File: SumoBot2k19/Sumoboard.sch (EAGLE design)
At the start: 37 parts

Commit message: began routing on PCB, moved components around for extra clarity, learned how to align things
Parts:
- added SWITCH: (no value), SparkFun-Connectors:CONN_03
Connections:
- removed net VIN1: C10.1
- removed net VIN2: C11.1
- removed net VIN3: C12.1
- new net VBAT: BATTERY-1.S, SWITCH.1
- net LEFT_DIR: now also B1.9*/RX2; no longer B1.2
- net LEFT_PWM: now also B1.8/TX3; no longer B1.3*
- net RIGHT_DIR: now also B1.3*; no longer B1.8/TX3
- net RIGHT_PWM: now also B1.2; no longer B1.9*/RX2
- net VIN: now also C10.1, C11.1, C12.1, SWITCH.2; no longer BATTERY-1.S
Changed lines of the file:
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@@
 <part name="BATTERY" library="Rembrandt Electronics - JST XH Connectors v1-0" deviceset="JST-XH-02-PIN" device="-LONG-PAD"/>
 <part name="GND1" library="audio amplifier example" library_urn="urn:adsk.eagle:library:970892" deviceset="GND" device="" value="SUP"/>
+<part name="SWITCH" library="SparkFun-Connectors" library_urn="urn:adsk.eagle:library:513" deviceset="CONN_03" device="" package3d_urn="urn:adsk.eagle:package:38063/1"/>
 </parts>
 <sheets>
@@
 </instance>
 <instance part="GND1" gate="G$1" x="147.32" y="20.32" smashed="yes"/>
+<instance part="SWITCH" gate="J$1" x="132.08" y="40.64" smashed="yes">
+<attribute name="VALUE" x="129.54" y="33.274" size="1.778" layer="96" font="vector"/>
+<attribute name="NAME" x="129.54" y="46.228" size="1.778" layer="95" font="vector"/>
+</instance>
 </instances>
 <busses>
@@
 <junction x="78.74" y="96.52"/>
 <label x="78.74" y="96.52" size="1.778" layer="95"/>
+<pinref part="C12" gate="G$1" pin="1"/>
+<wire x1="81.28" y1="96.52" x2="78.74" y2="96.52" width="0.1524" layer="91"/>
 </segment>
 <segment>
@@
 <junction x="78.74" y="76.2"/>
 <label x="78.74" y="76.2" size="1.778" layer="95"/>
+<pinref part="C11" gate="G$1" pin="1"/>
+<wire x1="81.28" y1="76.2" x2="78.74" y2="76.2" width="0.1524" layer="91"/>
 </segment>
 <segment>
@@
 <junction x="78.74" y="55.88"/>
 <label x="78.74" y="55.88" size="1.778" layer="95"/>
+<pinref part="C10" gate="G$1" pin="1"/>
+<wire x1="81.28" y1="55.88" x2="78.74" y2="55.88" width="0.1524" layer="91"/>
 </segment>
 <segment>
@@
 </segment>
 <segment>
-<pinref part="BATTERY" gate="-1" pin="S"/>
-<junction x="147.32" y="22.86"/>
-<label x="142.24" y="22.86" size="1.778" layer="95"/>
+<pinref part="SWITCH" gate="J$1" pin="2"/>
+<junction x="139.7" y="40.64"/>
+<label x="139.7" y="40.64" size="1.778" layer="95"/>
 </segment>
 </net>
@@
 <net name="RIGHT_DIR" class="0">
 <segment>
-<pinref part="B1" gate="G$1" pin="8/TX3"/>
-<junction x="30.48" y="66.04"/>
-<label x="30.48" y="66.04" size="1.778" layer="95"/>
-<wire x1="43.18" y1="66.04" x2="30.48" y2="66.04" width="0.1524" layer="91"/>
-</segment>
-<segment>
 <pinref part="SV5" gate="G$1" pin="2"/>
 <junction x="60.96" y="60.96"/>
@@
 <label x="48.26" y="40.64" size="1.778" layer="95"/>
 <wire x1="48.26" y1="40.64" x2="60.96" y2="40.64" width="0.1524" layer="91"/>
-</segment>
-</net>
-<net name="LEFT_DIR" class="0">
-<segment>
-<pinref part="B1" gate="G$1" pin="2"/>
-<junction x="30.48" y="81.28"/>
-<label x="30.48" y="81.28" size="1.778" layer="95"/>
-<wire x1="40.64" y1="81.28" x2="30.48" y2="81.28" width="0.1524" layer="91"/>
-</segment>
-<segment>
-<pinref part="SV7" gate="G$1" pin="2"/>
-<junction x="60.96" y="101.6"/>
-<label x="48.26" y="101.6" size="1.778" layer="95"/>
-<wire x1="60.96" y1="101.6" x2="48.26" y2="101.6" width="0.1524" layer="91"/>
-</segment>
-<segment>
-<pinref part="SV3" gate="G$1" pin="2"/>
-<junction x="60.96" y="81.28"/>
-<label x="48.26" y="81.28" size="1.778" layer="95"/>
-<wire x1="48.26" y1="81.28" x2="60.96" y2="81.28" width="0.1524" layer="91"/>
-</segment>
-</net>
-<net name="VOUT_IR" class="0">
-<segment>
-<pinref part="IR_RECEIVER" gate="J$1" pin="1"/>
-<junction x="162.56" y="38.1"/>
-<label x="162.56" y="38.1" size="1.778" layer="95"/>
-</segment>
-<segment>
-<pinref part="B1" gate="G$1" pin="12/DIN"/>
-<junction x="30.48" y="48.26"/>
-<label x="30.48" y="48.26" size="1.778" layer="95"/>
-<wire x1="40.64" y1="48.26" x2="30.48" y2="48.26" width="0.1524" layer="91"/>
-</segment>
-</net>
-<net name="VIN1" class="0">
-<segment>
-<pinref part="C10" gate="G$1" pin="1"/>
-<wire x1="78.74" y1="55.88" x2="81.28" y2="55.88" width="0.1524" layer="91"/>
-</segment>
-</net>
-<net name="VIN2" class="0">
-<segment>
-<pinref part="C11" gate="G$1" pin="1"/>
-<wire x1="78.74" y1="76.2" x2="81.28" y2="76.2" width="0.1524" layer="91"/>
-</segment>
-</net>
-<net name="VIN3" class="0">
-<segment>
-<pinref part="C12" gate="G$1" pin="1"/>
-<wire x1="78.74" y1="96.52" x2="81.28" y2="96.52" width="0.1524" layer="91"/>
-</segment>
-</net>
-<net name="LEFT_PWM" class="0">
-<segment>
-<pinref part="SV7" gate="G$1" pin="1"/>
-<junction x="60.96" y="104.14"/>
-<label x="48.26" y="104.14" size="1.778" layer="95"/>
-<wire x1="48.26" y1="104.14" x2="60.96" y2="104.14" width="0.1524" layer="91"/>
-</segment>
-<segment>
-<pinref part="SV3" gate="G$1" pin="1"/>
-<junction x="60.96" y="83.82"/>
-<label x="48.26" y="83.82" size="1.778" layer="95"/>
-<wire x1="48.26" y1="83.82" x2="60.96" y2="83.82" width="0.1524" layer="91"/>
 </segment>
 <segment>
@@
 </segment>
 </net>
+<net name="LEFT_DIR" class="0">
+<segment>
+<pinref part="SV7" gate="G$1" pin="2"/>
+<junction x="60.96" y="101.6"/>
+<label x="48.26" y="101.6" size="1.778" layer="95"/>
+<wire x1="60.96" y1="101.6" x2="48.26" y2="101.6" width="0.1524" layer="91"/>
+</segment>
+<segment>
+<pinref part="SV3" gate="G$1" pin="2"/>
+<junction x="60.96" y="81.28"/>
+<label x="48.26" y="81.28" size="1.778" layer="95"/>
+<wire x1="48.26" y1="81.28" x2="60.96" y2="81.28" width="0.1524" layer="91"/>
+</segment>
+<segment>
+<pinref part="B1" gate="G$1" pin="9*/RX2"/>
+<junction x="30.48" y="63.5"/>
+<label x="30.48" y="63.5" size="1.778" layer="95"/>
+<wire x1="38.1" y1="63.5" x2="30.48" y2="63.5" width="0.1524" layer="91"/>
+</segment>
+</net>
+<net name="VOUT_IR" class="0">
+<segment>
+<pinref part="IR_RECEIVER" gate="J$1" pin="1"/>
+<junction x="162.56" y="38.1"/>
+<label x="162.56" y="38.1" size="1.778" layer="95"/>
+</segment>
+<segment>
+<pinref part="B1" gate="G$1" pin="12/DIN"/>
+<junction x="30.48" y="48.26"/>
+<label x="30.48" y="48.26" size="1.778" layer="95"/>
+<wire x1="40.64" y1="48.26" x2="30.48" y2="48.26" width="0.1524" layer="91"/>
+</segment>
+</net>
+<net name="LEFT_PWM" class="0">
+<segment>
+<pinref part="SV7" gate="G$1" pin="1"/>
+<junction x="60.96" y="104.14"/>
+<label x="48.26" y="104.14" size="1.778" layer="95"/>
+<wire x1="48.26" y1="104.14" x2="60.96" y2="104.14" width="0.1524" layer="91"/>
+</segment>
+<segment>
+<pinref part="SV3" gate="G$1" pin="1"/>
+<junction x="60.96" y="83.82"/>
+<label x="48.26" y="83.82" size="1.778" layer="95"/>
+<wire x1="48.26" y1="83.82" x2="60.96" y2="83.82" width="0.1524" layer="91"/>
+</segment>
+<segment>
+<pinref part="B1" gate="G$1" pin="8/TX3"/>
+<junction x="30.48" y="66.04"/>
+<label x="30.48" y="66.04" size="1.778" layer="95"/>
+<wire x1="43.18" y1="66.04" x2="30.48" y2="66.04" width="0.1524" layer="91"/>
+</segment>
+</net>
 <net name="RIGHT_PWM" class="0">
 <segment>
@@
 </segment>
 <segment>
-<pinref part="B1" gate="G$1" pin="9*/RX2"/>
-<junction x="30.48" y="63.5"/>
-<label x="30.48" y="63.5" size="1.778" layer="95"/>
-<wire x1="38.1" y1="63.5" x2="30.48" y2="63.5" width="0.1524" layer="91"/>
+<pinref part="B1" gate="G$1" pin="2"/>
+<junction x="30.48" y="81.28"/>
+<label x="30.48" y="81.28" size="1.778" layer="95"/>
+<wire x1="40.64" y1="81.28" x2="30.48" y2="81.28" width="0.1524" layer="91"/>
 </segment>
 </net>
@@
 </segment>
 </net>
+<net name="VBAT" class="0">
+<segment>
+<pinref part="SWITCH" gate="J$1" pin="1"/>
+<junction x="139.7" y="38.1"/>
+<label x="139.7" y="38.1" size="1.778" layer="95"/>
+</segment>
+<segment>
+<pinref part="BATTERY" gate="-1" pin="S"/>
+<junction x="147.32" y="22.86"/>
+<label x="142.24" y="22.86" size="1.778" layer="95"/>
+</segment>
+</net>

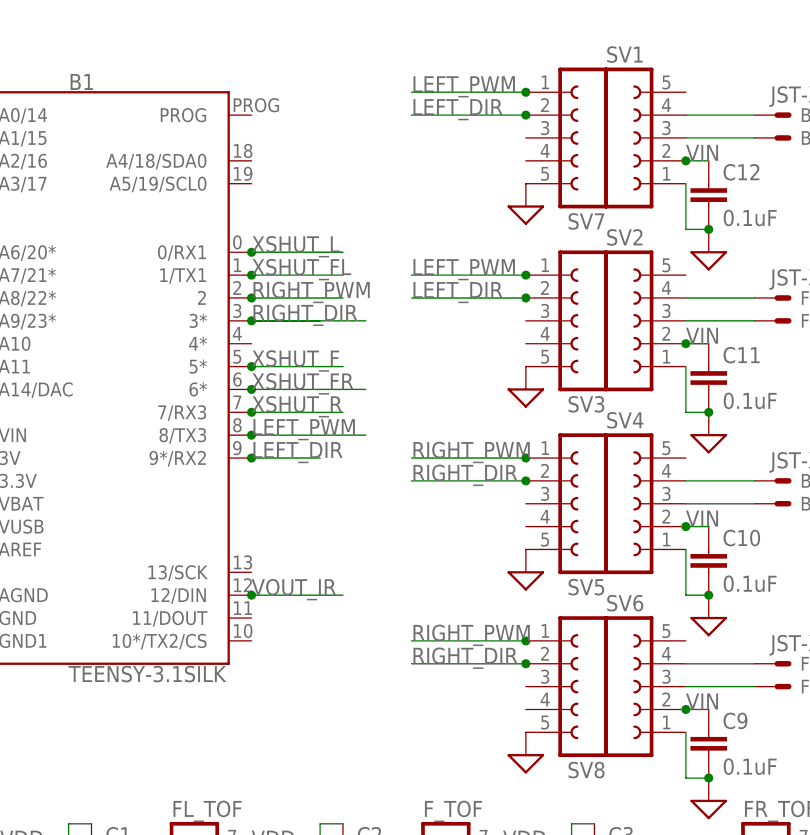
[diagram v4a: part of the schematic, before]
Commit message: trying to change the left/right pwm/direction pins
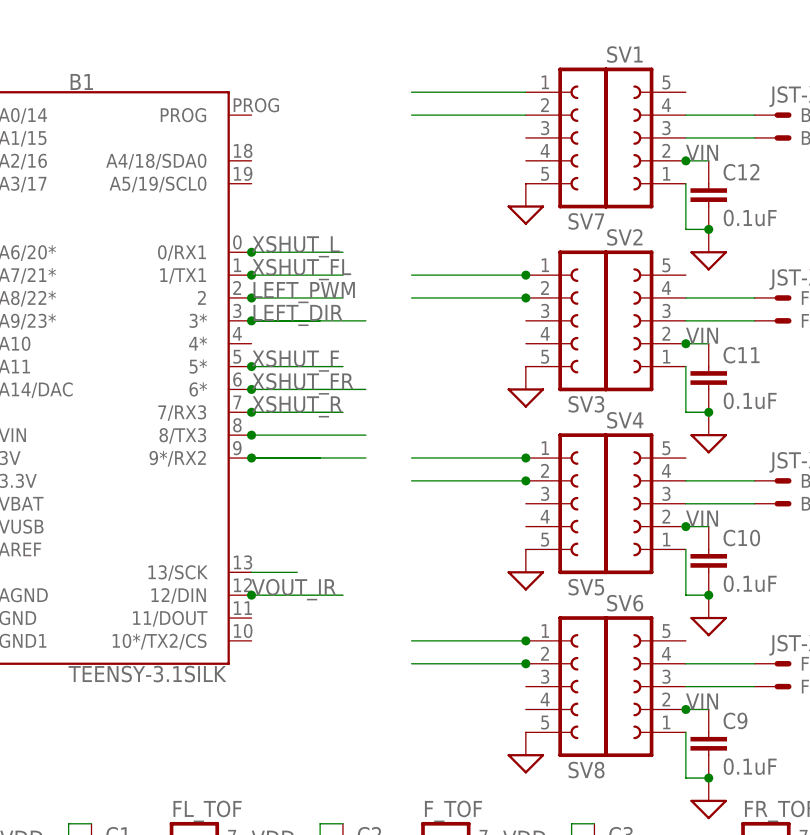
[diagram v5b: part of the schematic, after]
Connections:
- new net RIGHT: B1.13/SCK
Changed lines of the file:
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@@
 <setting verticaltext="up"/>
 </settings>
-<grid distance="0.1" unitdist="inch" unit="inch" style="lines" multiple="1" display="no" altdistance="0.01" altunitdist="inch" altunit="inch"/>
+<grid distance="0.1" unitdist="inch" unit="inch" style="lines" multiple="1" display="yes" altdistance="0.01" altunitdist="inch" altunit="inch"/>
 <layers>
 <layer number="1" name="Top" color="4" fill="1" visible="no" active="no"/>
@@
 <layer number="91" name="Nets" color="2" fill="1" visible="yes" active="yes"/>
 <layer number="92" name="Busses" color="1" fill="1" visible="yes" active="yes"/>
-<layer number="93" name="Pins" color="2" fill="1" visible="no" active="yes"/>
+<layer number="93" name="Pins" color="2" fill="1" visible="yes" active="yes"/>
 <layer number="94" name="Symbols" color="4" fill="1" visible="yes" active="yes"/>
 <layer number="95" name="Names" color="7" fill="1" visible="yes" active="yes"/>
@@
 <pinref part="SV5" gate="G$1" pin="2"/>
 <junction x="60.96" y="60.96"/>
-<label x="48.26" y="60.96" size="1.778" layer="95"/>
 <wire x1="48.26" y1="60.96" x2="60.96" y2="60.96" width="0.1524" layer="91"/>
 </segment>
@@
 <pinref part="SV8" gate="G$1" pin="2"/>
 <junction x="60.96" y="40.64"/>
-<label x="48.26" y="40.64" size="1.778" layer="95"/>
 <wire x1="48.26" y1="40.64" x2="60.96" y2="40.64" width="0.1524" layer="91"/>
 </segment>
@@
 <pinref part="B1" gate="G$1" pin="3*"/>
 <junction x="30.48" y="78.74"/>
-<label x="30.48" y="78.74" size="1.778" layer="95"/>
 <wire x1="38.1" y1="78.74" x2="30.48" y2="78.74" width="0.1524" layer="91"/>
 <wire x1="43.18" y1="78.74" x2="30.48" y2="78.74" width="0.1524" layer="91"/>
@@
 <segment>
 <pinref part="SV7" gate="G$1" pin="2"/>
-<junction x="60.96" y="101.6"/>
-<label x="48.26" y="101.6" size="1.778" layer="95"/>
 <wire x1="60.96" y1="101.6" x2="48.26" y2="101.6" width="0.1524" layer="91"/>
 </segment>
@@
 <pinref part="SV3" gate="G$1" pin="2"/>
 <junction x="60.96" y="81.28"/>
-<label x="48.26" y="81.28" size="1.778" layer="95"/>
 <wire x1="48.26" y1="81.28" x2="60.96" y2="81.28" width="0.1524" layer="91"/>
 </segment>
 <segment>
 <pinref part="B1" gate="G$1" pin="9*/RX2"/>
+<label x="30.48" y="78.74" size="1.778" layer="95"/>
+<wire x1="38.1" y1="63.5" x2="30.48" y2="63.5" width="0.1524" layer="91"/>
 <junction x="30.48" y="63.5"/>
-<label x="30.48" y="63.5" size="1.778" layer="95"/>
-<wire x1="38.1" y1="63.5" x2="30.48" y2="63.5" width="0.1524" layer="91"/>
+<wire x1="30.48" y1="63.5" x2="43.18" y2="63.5" width="0.1524" layer="91"/>
 </segment>
 </net>
@@
 <segment>
 <pinref part="SV7" gate="G$1" pin="1"/>
-<junction x="60.96" y="104.14"/>
-<label x="48.26" y="104.14" size="1.778" layer="95"/>
 <wire x1="48.26" y1="104.14" x2="60.96" y2="104.14" width="0.1524" layer="91"/>
 </segment>
@@
 <pinref part="SV3" gate="G$1" pin="1"/>
 <junction x="60.96" y="83.82"/>
-<label x="48.26" y="83.82" size="1.778" layer="95"/>
 <wire x1="48.26" y1="83.82" x2="60.96" y2="83.82" width="0.1524" layer="91"/>
 </segment>
 <segment>
 <pinref part="B1" gate="G$1" pin="8/TX3"/>
+<label x="30.48" y="81.28" size="1.778" layer="95"/>
+<wire x1="43.18" y1="66.04" x2="30.48" y2="66.04" width="0.1524" layer="91"/>
 <junction x="30.48" y="66.04"/>
-<label x="30.48" y="66.04" size="1.778" layer="95"/>
-<wire x1="43.18" y1="66.04" x2="30.48" y2="66.04" width="0.1524" layer="91"/>
 </segment>
 </net>
@@
 <pinref part="SV5" gate="G$1" pin="1"/>
 <junction x="60.96" y="63.5"/>
-<label x="48.26" y="63.5" size="1.778" layer="95"/>
 <wire x1="48.26" y1="63.5" x2="60.96" y2="63.5" width="0.1524" layer="91"/>
 </segment>
@@
 <pinref part="SV8" gate="G$1" pin="1"/>
 <junction x="60.96" y="43.18"/>
-<label x="48.26" y="43.18" size="1.778" layer="95"/>
 <wire x1="48.26" y1="43.18" x2="60.96" y2="43.18" width="0.1524" layer="91"/>
 </segment>
@@
 <pinref part="B1" gate="G$1" pin="2"/>
 <junction x="30.48" y="81.28"/>
-<label x="30.48" y="81.28" size="1.778" layer="95"/>
 <wire x1="40.64" y1="81.28" x2="30.48" y2="81.28" width="0.1524" layer="91"/>
 </segment>
@@
 </segment>
 </net>
+<net name="RIGHT" class="0">
+<segment>
+<pinref part="B1" gate="G$1" pin="13/SCK"/>
+<wire x1="30.48" y1="50.8" x2="35.56" y2="50.8" width="0.1524" layer="91"/>
+</segment>
+</net>
